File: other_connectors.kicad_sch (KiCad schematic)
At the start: 1 part

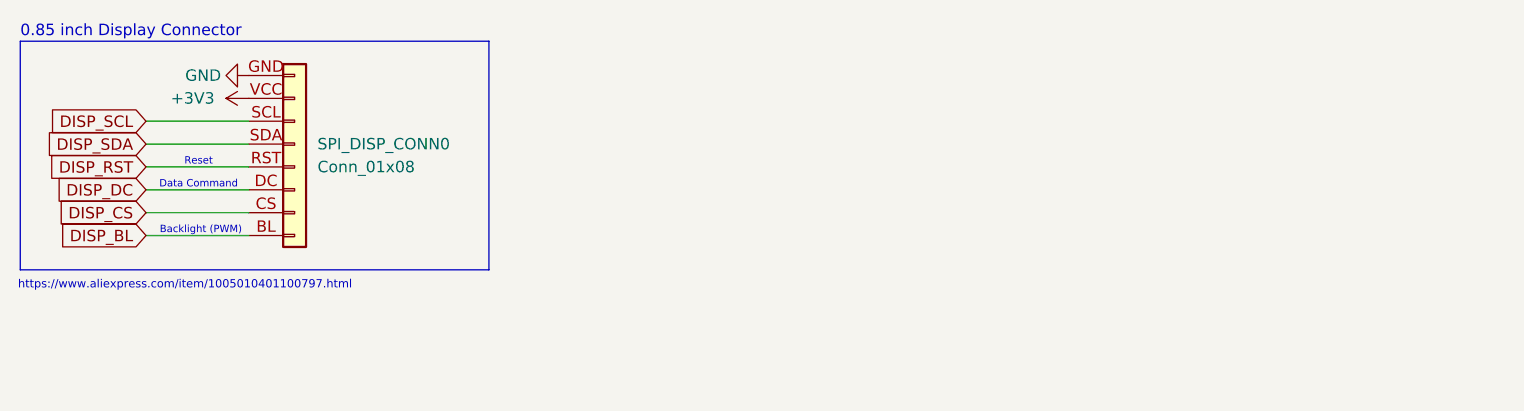
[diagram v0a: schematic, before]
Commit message: Changed to touchscreen LCD and added connectors for front breakout
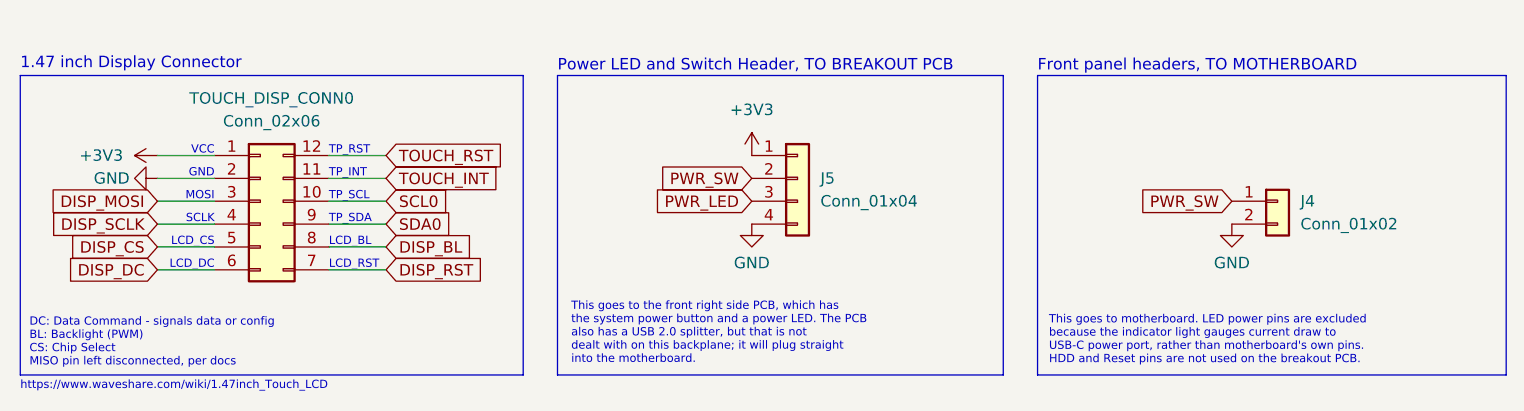
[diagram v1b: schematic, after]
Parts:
- removed SPI_DISP_CONN0: Conn_01x08, symbol Connector_Generic:Conn_01x08
- added J4: Conn_01x02, Connector_PinHeader_2.54mm:PinHeader_1x02_P2.54mm_Vertical_SMD_Pin1Left, symbol Connector_Generic:Conn_01x02
- added J5: Conn_01x04, Connector_PinSocket_2.54mm:PinSocket_1x04_P2.54mm_Horizontal, symbol Connector_Generic:Conn_01x04
- added TOUCH_DISP_CONN0: Conn_02x06, Connector_PinSocket_2.54mm:PinSocket_2x06_P2.54mm_Vertical_SMD, symbol Connector_Generic:Conn_02x06_Counter_Clockwise
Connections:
- net +3V3: now also J5.1 (Pin_1), TOUCH_DISP_CONN0.1 (Pin_1)
- net DISP_BL: now also TOUCH_DISP_CONN0.8 (Pin_8)
- net DISP_CS: now also TOUCH_DISP_CONN0.5 (Pin_5)
- net DISP_DC: now also TOUCH_DISP_CONN0.6 (Pin_6)
- net DISP_RST: now also TOUCH_DISP_CONN0.7 (Pin_7)
- net GND: now also J4.2 (Pin_2), J5.4 (Pin_4), TOUCH_DISP_CONN0.2 (Pin_2)
- new net DISP_MOSI: TOUCH_DISP_CONN0.3 (Pin_3)
- new net DISP_SCLK: TOUCH_DISP_CONN0.4 (Pin_4)
- new net PWR_LED: J5.3 (Pin_3)
- new net PWR_SW: J4.1 (Pin_1), J5.2 (Pin_2)
- new net SCL0: TOUCH_DISP_CONN0.10 (Pin_10)
- new net SDA0: TOUCH_DISP_CONN0.9 (Pin_9)
- new net TOUCH_INT: TOUCH_DISP_CONN0.11 (Pin_11)
- new net TOUCH_RST: TOUCH_DISP_CONN0.12 (Pin_12)
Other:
- note added: "1.47 inch Display Connector"
- note added: "DC: Data Command - signals data or config BL: Backlight (PWM) CS: Chip Select MISO pin left disconnected, per docs"
- note added: "Front panel headers, TO MOTHERBOARD"
- note added: "GND"
- note added: "LCD_BL"
- note added: "LCD_CS"
- note added: "LCD_DC"
- note added: "LCD_RST"
- note added: "MOSI"
- note added: "Power LED and Switch Header, TO BREAKOUT PCB"
- note added: "SCLK"
- note added: "TP_INT"
- note added: "TP_RST"
- note added: "TP_SCL"
- note added: "TP_SDA"
- note added: "This goes to motherboard. LED power pins are excluded because the indicator light gauges current draw to USB-C power port, rather than motherboard's own pins. HDD and Reset pins are not used on the breakout PCB."
- note added: "This goes to the front right side PCB, which has the system power button and a power LED. The PCB also has a USB 2.0 splitter, but that is not dealt with on this backplane; it will plug straight into the motherboard."
- note added: "VCC"
- note added: "https://www.waveshare.com/wiki/1.47inch_Touch_LCD"
- note removed: "0.85 inch Display Connector"
- note removed: "Backlight (PWM)"
- note removed: "Data Command"
- note removed: "Reset"
- note removed: "https://www.aliexpress.com/item/1005010401100797.html"

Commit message: Updated front breakout connector to 5V VCC with 2 more 5V pins to support higher current
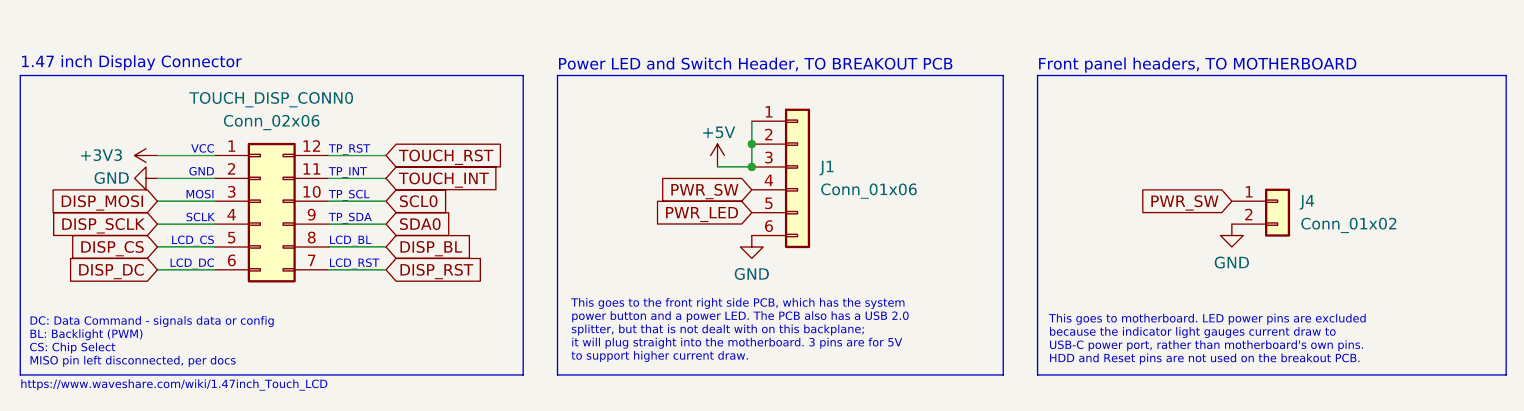
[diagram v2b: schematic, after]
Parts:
- removed J5: Conn_01x04, Connector_PinSocket_2.54mm:PinSocket_1x04_P2.54mm_Horizontal, symbol Connector_Generic:Conn_01x04
- added J1: Conn_01x06, Connector_PinSocket_2.54mm:PinSocket_1x06_P2.54mm_Horizontal, symbol Connector_Generic:Conn_01x06
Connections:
- net GND: now also J1.6 (Pin_6)
- net PWR_LED: now also J1.5 (Pin_5)
- net PWR_SW: now also J1.4 (Pin_4)
- new net +5V: J1.1 (Pin_1), J1.2 (Pin_2), J1.3 (Pin_3)
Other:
- note added: "This goes to the front right side PCB, which has the system power button and a power LED. The PCB also has a USB 2.0 splitter, but that is not dealt with on this backplane; it will plug straight into the motherboard. 3 pins are for 5V to support higher current draw."
- note removed: "This goes to the front right side PCB, which has the system power button and a power LED. The PCB also has a USB 2.0 splitter, but that is not dealt with on this backplane; it will plug straight into the motherboard."
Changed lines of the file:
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@@
 		)
 	)
-	(text "This goes to the front right side PCB, which has\nthe system power button and a power LED. The PCB\nalso has a USB 2.0 splitter, but that is not\ndealt with on this backplane; it will plug straight\ninto the motherboard."
-		(exclude_from_sim no)
-		(at 81.534 50.292 0)
+	(text "This goes to the front right side PCB, which has the system \npower button and a power LED. The PCB also has a USB 2.0\nsplitter, but that is not dealt with on this backplane;\nit will plug straight into the motherboard. 3 pins are for 5V\nto support higher current draw."
+		(exclude_from_sim no)
+		(at 81.534 50.038 0)
 		(effects
 			(font
@@
 		)
 	)
+	(junction
+		(at 101.6 31.75)
+		(diameter 0)
+		(color 0 0 0 0)
+	)
+	(junction
+		(at 101.6 29.21)
+		(diameter 0)
+		(color 0 0 0 0)
+	)
 	(wire
 		(pts
@@
 	(wire
 		(pts
+			(xy 97.79 31.75) (xy 101.6 31.75)
+		)
+		(stroke
+			(width 0)
+			(type default)
+		)
+	)
+	(wire
+		(pts
 			(xy 35.56 33.02) (xy 41.91 33.02)
+		)
+		(stroke
+			(width 0)
+			(type default)
+		)
+	)
+	(wire
+		(pts
+			(xy 101.6 29.21) (xy 101.6 31.75)
+		)
+		(stroke
+			(width 0)
+			(type default)
+		)
+	)
+	(wire
+		(pts
+			(xy 101.6 26.67) (xy 101.6 29.21)
 		)
 		(stroke
@@
 	(global_label "PWR_SW"
 		(shape input)
-		(at 101.6 33.02 180)
+		(at 101.6 34.29 180)
 		(fields_autoplaced yes)
 		(effects
@@
 		)
 		(property "Intersheetrefs" "${INTERSHEET_REFS}"
-			(at 90.9949 33.02 0)
+			(at 90.9949 34.29 0)
 			(hide yes)
 			(show_name no)
@@
 	(global_label "PWR_LED"
 		(shape input)
-		(at 101.6 35.56 180)
+		(at 101.6 36.83 180)
 		(fields_autoplaced yes)
 		(effects
@@
 		)
 		(property "Intersheetrefs" "${INTERSHEET_REFS}"
-			(at 90.2087 35.56 0)
+			(at 90.2087 36.83 0)
 			(hide yes)
 			(show_name no)
@@
 		)
 		(instances
+			(project "other_connectors"
+				(path "/9b94df28-2798-4b39-aed9-30882f1bc4a5"
+					(reference "#PWR0143")
+					(unit 1)
+				)
+			)
 			(project "serverv2_backplane"
 				(path "/a6fda882-b5b2-43b7-bcc8-365357a6eb10"
@@
 		)
 		(instances
+			(project "other_connectors"
+				(path "/9b94df28-2798-4b39-aed9-30882f1bc4a5"
+					(reference "#PWR0140")
+					(unit 1)
+				)
+			)
 			(project "serverv2_backplane"
 				(path "/a6fda882-b5b2-43b7-bcc8-365357a6eb10"
@@
 	(symbol
 		(lib_id "power:+1V1")
-		(at 101.6 30.48 0)
+		(at 97.79 31.75 0)
 		(unit 1)
 		(body_style 1)
@@
 		(in_pos_files yes)
 		(dnp no)
-		(fields_autoplaced yes)
 		(property "Reference" "#PWR0124"
-			(at 101.6 34.29 0)
-			(hide yes)
-			(show_name no)
-			(do_not_autoplace no)
-			(effects
-				(font
-					(size 1.27 1.27)
-				)
-			)
-		)
-		(property "Value" "+3V3"
-			(at 101.6 25.4 0)
-			(show_name no)
-			(do_not_autoplace no)
-			(effects
-				(font
-					(size 1.27 1.27)
-				)
+			(at 97.79 35.56 0)
+			(hide yes)
+			(show_name no)
+			(do_not_autoplace no)
+			(effects
+				(font
+					(size 1.27 1.27)
+				)
+			)
+		)
+		(property "Value" "+5V"
+			(at 96.012 27.94 0)
+			(show_name no)
+			(do_not_autoplace no)
+			(effects
+				(font
+					(size 1.27 1.27)
+				)
+				(justify left)
 			)
 		)
 		(property "Footprint" ""
-			(at 101.6 30.48 0)
+			(at 97.79 31.75 0)
 			(hide yes)
 			(show_name no)
@@
 		)
 		(property "Datasheet" ""
-			(at 101.6 30.48 0)
+			(at 97.79 31.75 0)
 			(hide yes)
 			(show_name no)
@@
 		)
 		(property "Description" "Power symbol creates a global label with name \"+1V1\""
-			(at 101.6 30.48 0)
+			(at 97.79 31.75 0)
 			(hide yes)
 			(show_name no)
@@
 		)
 		(instances
+			(project "other_connectors"
+				(path "/9b94df28-2798-4b39-aed9-30882f1bc4a5"
+					(reference "#PWR0124")
+					(unit 1)
+				)
+			)
 			(project "serverv2_backplane"
 				(path "/a6fda882-b5b2-43b7-bcc8-365357a6eb10"
@@
 		)
 		(instances
+			(project "other_connectors"
+				(path "/9b94df28-2798-4b39-aed9-30882f1bc4a5"
+					(reference "#PWR0141")
+					(unit 1)
+				)
+			)
 			(project "serverv2_backplane"
 				(path "/a6fda882-b5b2-43b7-bcc8-365357a6eb10"
@@
 		)
 		(instances
+			(project "other_connectors"
+				(path "/9b94df28-2798-4b39-aed9-30882f1bc4a5"
+					(reference "TOUCH_DISP_CONN0")
+					(unit 1)
+				)
+			)
 			(project "serverv2_backplane"
 				(path "/a6fda882-b5b2-43b7-bcc8-365357a6eb10"
@@
 	)
 	(symbol
-		(lib_id "Connector_Generic:Conn_01x04")
-		(at 106.68 33.02 0)
-		(unit 1)
-		(body_style 1)
-		(exclude_from_sim no)
-		(in_bom yes)
-		(on_board yes)
-		(in_pos_files yes)
-		(dnp no)
-		(fields_autoplaced yes)
-		(property "Reference" "J5"
-			(at 109.22 33.0199 0)
-			(show_name no)
-			(do_not_autoplace no)
-			(effects
-				(font
-					(size 1.27 1.27)
-				)
-				(justify left)
-			)
-		)
-		(property "Value" "Conn_01x04"
-			(at 109.22 35.5599 0)
-			(show_name no)
-			(do_not_autoplace no)
-			(effects
-				(font
-					(size 1.27 1.27)
-				)
-				(justify left)
-			)
-		)
-		(property "Footprint" "Connector_PinSocket_2.54mm:PinSocket_1x04_P2.54mm_Horizontal"
-			(at 106.68 33.02 0)
-			(hide yes)
-			(show_name no)
-			(do_not_autoplace no)
-			(effects
-				(font
-					(size 1.27 1.27)
-				)
-			)
-		)
-		(property "Datasheet" ""
-			(at 106.68 33.02 0)
-			(hide yes)
-			(show_name no)
-			(do_not_autoplace no)
-			(effects
-				(font
-					(size 1.27 1.27)
-				)
-			)
-		)
-		(property "Description" "Generic connector, single row, 01x04, script generated (kicad-library-utils/schlib/autogen/connector/)"
-			(at 106.68 33.02 0)
-			(hide yes)
-			(show_name no)
-			(do_not_autoplace no)
-			(effects
-				(font
-					(size 1.27 1.27)
-				)
-			)
-		)
-		(pin "4"
-		)
-		(pin "3"
-		)
-		(pin "2"
-		)
-		(pin "1"
-		)
-		(instances
-			(project "serverv2_backplane"
-				(path "/a6fda882-b5b2-43b7-bcc8-365357a6eb10"
-					(reference "J5")
-					(unit 1)
-				)
-			)
-		)
-	)
-	(symbol
 		(lib_id "power:GND")
-		(at 101.6 38.1 0)
+		(at 101.6 39.37 0)
 		(unit 1)
 		(body_style 1)
@@
 		(dnp no)
 		(property "Reference" "#PWR0142"
-			(at 101.6 44.45 0)
+			(at 101.6 45.72 0)
 			(hide yes)
 			(show_name no)
@@
 		)
 		(property "Value" "GND"
-			(at 101.6 42.418 0)
+			(at 101.6 43.688 0)
 			(show_name no)
 			(do_not_autoplace no)
@@
 		)
 		(property "Footprint" ""
-			(at 101.6 38.1 0)
+			(at 101.6 39.37 0)
 			(hide yes)
 			(show_name no)
@@
 		)
 		(property "Datasheet" ""
-			(at 101.6 38.1 0)
+			(at 101.6 39.37 0)
 			(hide yes)
 			(show_name no)
@@
 		)
 		(property "Description" "Power symbol creates a global label with name \"GND\" , ground"
-			(at 101.6 38.1 0)
+			(at 101.6 39.37 0)
 			(hide yes)
 			(show_name no)
@@
 		)
 		(instances
+			(project "other_connectors"
+				(path "/9b94df28-2798-4b39-aed9-30882f1bc4a5"
+					(reference "#PWR0142")
+					(unit 1)
+				)
+			)
 			(project "serverv2_backplane"
 				(path "/a6fda882-b5b2-43b7-bcc8-365357a6eb10"
@@
 		)
 		(instances
+			(project "other_connectors"
+				(path "/9b94df28-2798-4b39-aed9-30882f1bc4a5"
+					(reference "J4")
+					(unit 1)
+				)
+			)
 			(project "serverv2_backplane"
 				(path "/a6fda882-b5b2-43b7-bcc8-365357a6eb10"
@@
 					(unit 1)
 				)
+			)
+		)
+	)
+	(symbol
+		(lib_id "Connector_Generic:Conn_01x06")
+		(at 106.68 31.75 0)
+		(unit 1)
+		(body_style 1)
+		(exclude_from_sim no)
+		(in_bom yes)
+		(on_board yes)
+		(in_pos_files yes)
+		(dnp no)
+		(fields_autoplaced yes)
+		(property "Reference" "J1"
+			(at 109.22 31.7499 0)
+			(show_name no)
+			(do_not_autoplace no)
+			(effects
+				(font
+					(size 1.27 1.27)
+				)
+				(justify left)
+			)
+		)
+		(property "Value" "Conn_01x06"
+			(at 109.22 34.2899 0)
+			(show_name no)
+			(do_not_autoplace no)
+			(effects
+				(font
+					(size 1.27 1.27)
+				)
+				(justify left)
+			)
+		)
+		(property "Footprint" "Connector_PinSocket_2.54mm:PinSocket_1x06_P2.54mm_Horizontal"
+			(at 106.68 31.75 0)
+			(hide yes)
+			(show_name no)
+			(do_not_autoplace no)
+			(effects
+				(font
+					(size 1.27 1.27)
+				)
+			)
+		)
+		(property "Datasheet" ""
+			(at 106.68 31.75 0)
+			(hide yes)
+			(show_name no)
+			(do_not_autoplace no)
+			(effects
+				(font
+					(size 1.27 1.27)
+				)
+			)
+		)
+		(property "Description" "Generic connector, single row, 01x06, script generated (kicad-library-utils/schlib/autogen/connector/)"
+			(at 106.68 31.75 0)
+			(hide yes)
+			(show_name no)
+			(do_not_autoplace no)
+			(effects
+				(font
+					(size 1.27 1.27)
+				)
+			)
+		)
+		(pin "5"
+		)
+		(pin "6"
+		)
+		(pin "3"
+		)
+		(pin "2"
+		)
+		(pin "4"
+		)
+		(pin "1"
+		)
+		(instances
+			(project "other_connectors"
+				(path "/9b94df28-2798-4b39-aed9-30882f1bc4a5"
+					(reference "J1")
+					(unit 1)
+				)
